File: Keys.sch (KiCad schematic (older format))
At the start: 144 parts, among them SW1 20, SW10 LEFT-SHIFT, SW11 41, SW12 51, SW13 22, SW14 32, SW15 42, SW16 52, SW17 02, SW18 12, SW19 03, SW2 30, SW20 13, SW21 23, SW22 33, SW23 43, SW24 53, SW25 24, SW26 34, SW28 54, SW29 04, SW3 40, SW30 14, SW31 05, SW32 15, SW33 25, SW34 35, SW35 45, SW37 26, SW38 36, SW39 46, SW4 50, SW40 56, SW41 06, SW42 16, SW43 07, SW44 17, SW45 27, SW46 37, SW48 57, SW49 28, SW5 00, SW50 38, SW51 48, SW52 58, SW53 08, SW54 18, SW55 09, SW56 19, SW57 29, SW58 39, SW59 49, SW6 10, SW60 59, SW61 010, SW62 110, SW63 210, SW64 310, SW65 410, SW66 510, SW67 011, SW68 111, SW69 211, SW7 01, SW70 311, SW71 411, SW72 511, SW8 11, SW9 21

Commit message: iterating
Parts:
- Backspace1: renamed from SW60; footprint CherryKeys:CHERRY_PCB_100H -> daprice-keyswitches:Stabilizer_MX_2u; symbol Keys-rescue:SWITCH_PUSH-Cherry-Symbol-chgray-keyboard-rescue -> Keys-rescue:SWITCH_PUSH-Cherry-Symbol-chgray-keyboard-rescue-Keys-rescue
- D1, D10, D11, D12, D13, D14, D15, D16, D17, D18, D19, D2, D20, D21, D22, D23, D24, D25, D26, D27, D28, D29, D3, D30, D31, D32, D33, D34, D35, D36, D37, D38, D39, D4, D40, D41, D42, D43, D44, D45, D46, D47, D48, D49, D5, D50, D51, D52, D53, D54, D55, D56, D57, D58, D59, D6, D60, D61, D62, D63, D64, D65, D66, D67, D68, D69, D7, D70, D71, D72, D8, D9: footprint CherryKeys:CHERRY_MX_DIODE -> Diode_SMD:D_SOD-123; symbol Keys-rescue:DIODE-Cherry-Symbol-chgray-keyboard-rescue -> Keys-rescue:DIODE-Cherry-Symbol-chgray-keyboard-rescue-Keys-rescue
- ENTER1: renamed from SW67; footprint CherryKeys:CHERRY_PCB_100H -> daprice-keyswitches:Stabilizer_MX_2u; symbol Keys-rescue:SWITCH_PUSH-Cherry-Symbol-chgray-keyboard-rescue -> Keys-rescue:SWITCH_PUSH-Cherry-Symbol-chgray-keyboard-rescue-Keys-rescue
- LEFT-SHIFT1: renamed from SW10; value LEFT-SHIFT -> 31; footprint CherryKeys:CHERRY_PCB_100H -> daprice-keyswitches:Stabilizer_MX_2u; symbol Keys-rescue:SWITCH_PUSH-Cherry-Symbol-chgray-keyboard-rescue -> Keys-rescue:SWITCH_PUSH-Cherry-Symbol-chgray-keyboard-rescue-Keys-rescue
- LEFT-SPACE1, RIGHT-SHIFT1, RIGHT-SHIFT2: footprint CherryKeys:CHERRY_PCB_100H -> daprice-keyswitches:Stabilizer_MX_2u; symbol Keys-rescue:SWITCH_PUSH-Cherry-Symbol-chgray-keyboard-rescue -> Keys-rescue:SWITCH_PUSH-Cherry-Symbol-chgray-keyboard-rescue-Keys-rescue
- SW1, SW11, SW12, SW13, SW14, SW15, SW16, SW17, SW18, SW19, SW2, SW20, SW21, SW22, SW23, SW24, SW25, SW26, SW28, SW29, SW3, SW30, SW31, SW32, SW33, SW34, SW35, SW37, SW38, SW39, SW4, SW40, SW41, SW42, SW43, SW44, SW45, SW46, SW48, SW49, SW5, SW50, SW51, SW52, SW53, SW54, SW55, SW56, SW57, SW58, SW59, SW6, SW61, SW62, SW63, SW64, SW65, SW66, SW68, SW69, SW7, SW70, SW71, SW72, SW8, SW9: footprint CherryKeys:CHERRY_PCB_100H -> daprice-keyswitches:Kailh_socket_MX; symbol Keys-rescue:SWITCH_PUSH-Cherry-Symbol-chgray-keyboard-rescue -> Keys-rescue:SWITCH_PUSH-Cherry-Symbol-chgray-keyboard-rescue-Keys-rescue
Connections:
- wire segments 368 -> 372

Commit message: add 1.75U switch
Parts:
- Backspace1, ENTER1, LEFT-SHIFT1, LEFT-SPACE1, RIGHT-SHIFT1, RIGHT-SHIFT2, SW11, SW12, SW13, SW14, SW15, SW16, SW17, SW18, SW19, SW2, SW20, SW21, SW22, SW23, SW24, SW25, SW26, SW28, SW29, SW3, SW30, SW31, SW32, SW33, SW34, SW35, SW37, SW38, SW39, SW4, SW40, SW41, SW42, SW43, SW44, SW45, SW46, SW48, SW49, SW5, SW50, SW51, SW52, SW53, SW54, SW55, SW56, SW57, SW58, SW59, SW6, SW61, SW62, SW63, SW64, SW65, SW66, SW68, SW69, SW7, SW70, SW71, SW72, SW8, SW9: symbol Keys-rescue:SWITCH_PUSH-Cherry-Symbol-chgray-keyboard-rescue-Keys-rescue -> Keys-rescue:SWITCH_PUSH-Cherry-Symbol-chgray-keyboard-rescue-Keys-rescue-Keys-rescue
- D1, D10, D11, D12, D13, D14, D15, D16, D17, D18, D19, D2, D20, D21, D22, D23, D24, D25, D26, D27, D28, D29, D3, D30, D31, D32, D33, D34, D35, D36, D37, D38, D39, D4, D40, D41, D42, D43, D44, D45, D46, D47, D48, D49, D5, D50, D51, D52, D53, D54, D55, D56, D57, D58, D59, D6, D60, D61, D62, D63, D64, D65, D66, D67, D68, D69, D7, D70, D71, D72, D8, D9: symbol Keys-rescue:DIODE-Cherry-Symbol-chgray-keyboard-rescue-Keys-rescue -> Keys-rescue:DIODE-Cherry-Symbol-chgray-keyboard-rescue-Keys-rescue-Keys-rescue
- SW1: footprint daprice-keyswitches:Kailh_socket_MX -> daprice-keyswitches:Stabilizer_MX_1.75u; symbol Keys-rescue:SWITCH_PUSH-Cherry-Symbol-chgray-keyboard-rescue-Keys-rescue -> Keys-rescue:SWITCH_PUSH-Cherry-Symbol-chgray-keyboard-rescue-Keys-rescue-Keys-rescue

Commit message: working
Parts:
- SW6: footprint daprice-keyswitches:Kailh_socket_MX -> daprice-keyswitches:Stabilizer_MX_1.5u
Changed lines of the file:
@@
 F 0 "SW6" H 2150 2110 50  0000 C CNN
 F 1 "10" H 2000 1920 50  0000 C CNN
-F 2 "daprice-keyswitches:Kailh_socket_MX" H 2000 2000 60  0001 C CNN
+F 2 "daprice-keyswitches:Stabilizer_MX_1.5u" H 2000 2000 60  0001 C CNN
 F 3 "" H 2000 2000 60  0001 C CNN
 	1    2000 2000

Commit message: working on rgb
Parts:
- added D73, D74, D75, D76, D77, D78, D79, D80, D81, D82, D83, D84: DIODE, Diode_SMD:D_SOD-123, symbol chgray-keyboard-rescue:DIODE-Cherry-Symbol-chgray-keyboard-rescue-Keys-rescue-K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
- added ENTER2, ENTER3: 011, daprice-keyswitches:Stabilizer_MX_1.75u, symbol chgray-keyboard-rescue:SWITCH_PUSH-Cherry-Symbol-chgray-keyboard-rescue-Keys-re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
- added SW1, SW36: 111, daprice-keyswitches:Kailh_socket_MX, symbol chgray-keyboard-rescue:SWITCH_PUSH-Cherry-Symbol-chgray-keyboard-rescue-Keys-re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
- added SW10, SW60: 311, daprice-keyswitches:Kailh_socket_MX, symbol chgray-keyboard-rescue:SWITCH_PUSH-Cherry-Symbol-chgray-keyboard-rescue-Keys-re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
- added SW15, SW67: 411, daprice-keyswitches:Kailh_socket_MX, symbol chgray-keyboard-rescue:SWITCH_PUSH-Cherry-Symbol-chgray-keyboard-rescue-Keys-re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
- added SW27, SW73: 511, daprice-keyswitches:Kailh_socket_MX, symbol chgray-keyboard-rescue:SWITCH_PUSH-Cherry-Symbol-chgray-keyboard-rescue-Keys-re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
- added SW47, SW6: 211, daprice-keyswitches:Kailh_socket_MX, symbol chgray-keyboard-rescue:SWITCH_PUSH-Cherry-Symbol-chgray-keyboard-rescue-Keys-re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
- Backspace1: footprint daprice-keyswitches:Stabilizer_MX_2u -> daprice-keyswitches:Stabilizer_MX_1.25u; symbol Keys-rescue:SWITCH_PUSH-Cherry-Symbol-chgray-keyboard-rescue-Keys-rescue-Keys-rescue -> chgray-keyboard-rescue:SWITCH_PUSH-Cherry-Symbol-chgray-keyboard-rescue-Keys-rescue-Keys-rescue-Keys-rescue
- CAPS1: renamed from SW1; footprint daprice-keyswitches:Stabilizer_MX_1.75u -> daprice-keyswitches:Stabilizer_MX_1.5u; symbol Keys-rescue:SWITCH_PUSH-Cherry-Symbol-chgray-keyboard-rescue-Keys-rescue-Keys-rescue -> chgray-keyboard-rescue:SWITCH_PUSH-Cherry-Symbol-chgray-keyboard-rescue-Keys-rescue-Keys-rescue-Keys-rescue
- D1, D10, D11, D12, D13, D14, D15, D16, D17, D18, D19, D2, D20, D21, D22, D23, D24, D25, D26, D27, D28, D29, D3, D30, D31, D32, D33, D34, D35, D36, D37, D38, D39, D4, D40, D41, D42, D43, D44, D45, D46, D47, D48, D49, D5, D50, D51, D52, D53, D54, D55, D56, D57, D58, D59, D6, D60, D61, D62, D63, D64, D65, D66, D67, D68, D69, D7, D70, D71, D72, D8, D9: symbol Keys-rescue:DIODE-Cherry-Symbol-chgray-keyboard-rescue-Keys-rescue-Keys-rescue -> chgray-keyboard-rescue:DIODE-Cherry-Symbol-chgray-keyboard-rescue-Keys-rescue-Keys-rescue-Keys-rescue
- ENTER1: footprint daprice-keyswitches:Stabilizer_MX_2u -> daprice-keyswitches:Stabilizer_MX_1.75u; symbol Keys-rescue:SWITCH_PUSH-Cherry-Symbol-chgray-keyboard-rescue-Keys-rescue-Keys-rescue -> chgray-keyboard-rescue:SWITCH_PUSH-Cherry-Symbol-chgray-keyboard-rescue-Keys-rescue-Keys-rescue-Keys-rescue
- LEFT-SHIFT1, SW11, SW12, SW13, SW14, SW16, SW17, SW18, SW19, SW2, SW20, SW21, SW22, SW23, SW24, SW25, SW26, SW28, SW29, SW3, SW30, SW31, SW32, SW33, SW34, SW35, SW37, SW38, SW39, SW4, SW40, SW41, SW42, SW43, SW44, SW45, SW46, SW48, SW49, SW5, SW50, SW51, SW52, SW53, SW54, SW55, SW56, SW57, SW58, SW59, SW61, SW62, SW63, SW64, SW65, SW66, SW68, SW69, SW7, SW70, SW71, SW72, SW8, SW9: symbol Keys-rescue:SWITCH_PUSH-Cherry-Symbol-chgray-keyboard-rescue-Keys-rescue-Keys-rescue -> chgray-keyboard-rescue:SWITCH_PUSH-Cherry-Symbol-chgray-keyboard-rescue-Keys-rescue-Keys-rescue-Keys-rescue
- LEFT-SPACE1, RIGHT-SHIFT1: footprint daprice-keyswitches:Stabilizer_MX_2u -> daprice-keyswitches:Stabilizer_MX_2.25u; symbol Keys-rescue:SWITCH_PUSH-Cherry-Symbol-chgray-keyboard-rescue-Keys-rescue-Keys-rescue -> chgray-keyboard-rescue:SWITCH_PUSH-Cherry-Symbol-chgray-keyboard-rescue-Keys-rescue-Keys-rescue-Keys-rescue
- RIGHT-SPACE1: renamed from RIGHT-SHIFT2; footprint daprice-keyswitches:Stabilizer_MX_2u -> daprice-keyswitches:Stabilizer_MX_2.25u; symbol Keys-rescue:SWITCH_PUSH-Cherry-Symbol-chgray-keyboard-rescue-Keys-rescue-Keys-rescue -> chgray-keyboard-rescue:SWITCH_PUSH-Cherry-Symbol-chgray-keyboard-rescue-Keys-rescue-Keys-rescue-Keys-rescue
- TAB1: renamed from SW6; footprint daprice-keyswitches:Stabilizer_MX_1.5u -> daprice-keyswitches:Stabilizer_MX_1.25u; symbol Keys-rescue:SWITCH_PUSH-Cherry-Symbol-chgray-keyboard-rescue-Keys-rescue-Keys-rescue -> chgray-keyboard-rescue:SWITCH_PUSH-Cherry-Symbol-chgray-keyboard-rescue-Keys-rescue-Keys-rescue-Keys-rescue
- WinKey1: renamed from SW15; footprint daprice-keyswitches:Kailh_socket_MX -> daprice-keyswitches:Stabilizer_MX_1.5u; symbol Keys-rescue:SWITCH_PUSH-Cherry-Symbol-chgray-keyboard-rescue-Keys-rescue-Keys-rescue -> chgray-keyboard-rescue:SWITCH_PUSH-Cherry-Symbol-chgray-keyboard-rescue-Keys-rescue-Keys-rescue-Keys-rescue
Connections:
- net labels added: KEY_COL12, KEY_COL13
- wire segments 372 -> 434

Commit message: rgb
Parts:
- S1: renamed from ENTER1; footprint daprice-keyswitches:Stabilizer_MX_1.75u -> daprice-keyswitches:Kailh_socket_MX
- S2: renamed from ENTER2; footprint daprice-keyswitches:Stabilizer_MX_1.75u -> daprice-keyswitches:Kailh_socket_MX
- S3: renamed from ENTER3; footprint daprice-keyswitches:Stabilizer_MX_1.75u -> daprice-keyswitches:Kailh_socket_MX
- renumbered SW2 to SW1, SW13 to SW10, SW14 to SW11, SW16 to SW12, SW17 to SW13, SW18 to SW14, SW19 to SW15, SW20 to SW16, SW21 to SW17, SW22 to SW18, SW23 to SW19, SW3 to SW2, SW24 to SW20, SW25 to SW21, SW26 to SW22, SW28 to SW23, SW29 to SW24, SW30 to SW25, SW31 to SW26, SW32 to SW27, SW33 to SW28, SW34 to SW29, SW4 to SW3, SW35 to SW30, SW37 to SW31, SW38 to SW32, SW39 to SW33, SW40 to SW34, SW41 to SW35, SW42 to SW36, SW43 to SW37, SW44 to SW38, SW45 to SW39, SW5 to SW4, SW46 to SW40, SW48 to SW41, SW49 to SW42, SW50 to SW43, SW51 to SW44, SW52 to SW45, SW53 to SW46, SW54 to SW47, SW55 to SW48, SW56 to SW49, SW7 to SW5, SW57 to SW50, SW58 to SW51, SW59 to SW52, SW61 to SW53, SW62 to SW54, SW63 to SW55, SW64 to SW56, SW65 to SW57, SW66 to SW58, SW68 to SW59, SW8 to SW6, SW69 to SW60, SW70 to SW61, SW71 to SW62, SW72 to SW63, SW1 to SW64, SW6 to SW65, SW10 to SW66, SW15 to SW67, SW27 to SW68, SW36 to SW69, SW9 to SW7, SW47 to SW70, SW60 to SW71, SW67 to SW72, SW11 to SW8, SW12 to SW9

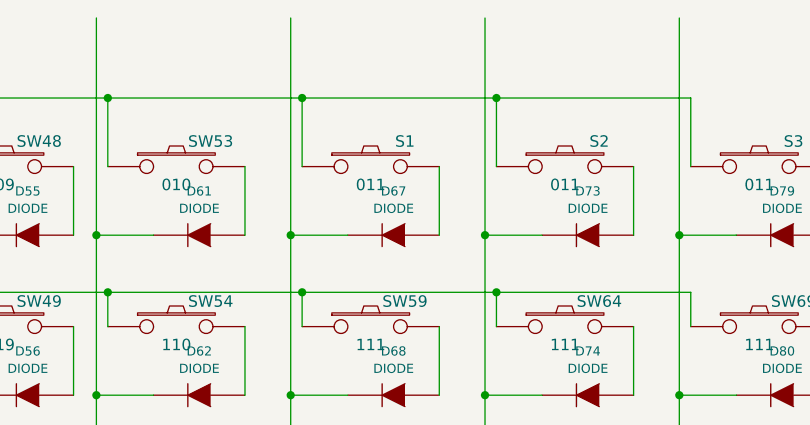
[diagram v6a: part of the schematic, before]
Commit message: laying out keyboard; all keys aligned!
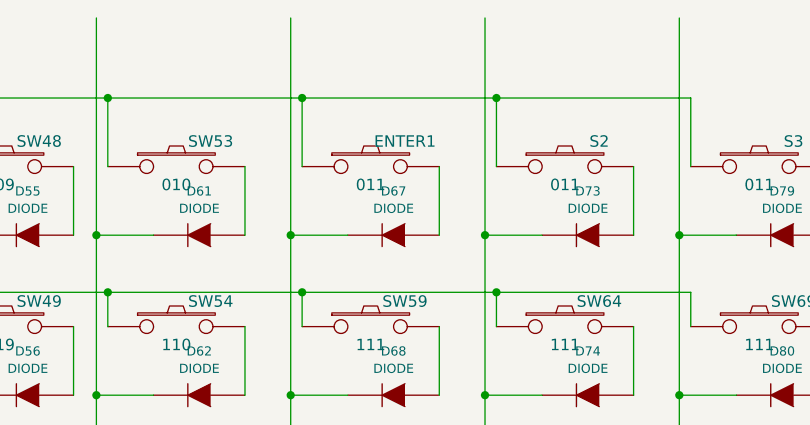
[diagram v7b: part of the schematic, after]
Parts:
- ENTER1: renamed from S1; footprint daprice-keyswitches:Kailh_socket_MX -> daprice-keyswitches:Stabilizer_MX_1.75u
- SW44: footprint daprice-keyswitches:Kailh_socket_MX -> daprice-keyswitches:Stabilizer_MX_1.25u
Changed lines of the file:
@@
 F 0 "SW44" H 9300 4960 50  0000 C CNN
 F 1 "48" H 9150 4770 50  0000 C CNN
-F 2 "daprice-keyswitches:Kailh_socket_MX" H 9150 4850 60  0001 C CNN
+F 2 "daprice-keyswitches:Stabilizer_MX_1.25u" H 9150 4850 60  0001 C CNN
 F 3 "" H 9150 4850 60  0001 C CNN
 	1    9150 4850
@@
 Connection ~ 10350 2300
 $Comp
-L chgray-keyboard-rescue:SWITCH_PUSH-Cherry-Symbol-chgray-keyboard-rescue-Keys-rescue-Keys-rescue-Keys-rescue S1
+L chgray-keyboard-rescue:SWITCH_PUSH-Cherry-Symbol-chgray-keyboard-rescue-Keys-rescue-Keys-rescue-Keys-rescue ENTER1
 U 1 1 60AE6AA1
 P 11550 1300
-F 0 "S1" H 11700 1410 50  0000 C CNN
+F 0 "ENTER1" H 11700 1410 50  0000 C CNN
 F 1 "011" H 11550 1220 50  0000 C CNN
-F 2 "daprice-keyswitches:Kailh_socket_MX" H 11550 1300 60  0001 C CNN
+F 2 "daprice-keyswitches:Stabilizer_MX_1.75u" H 11550 1300 60  0001 C CNN
 F 3 "" H 11550 1300 60  0001 C CNN
 	1    11550 1300

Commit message: Squashed commit of the following:
commit 82315f0ae1d56e508510c236d094091e5279ecfb
Author: Chris Gray (COSINE FUNDAMENTALS) <chgray@microsoft.com>
Date:   Sun May 9 12:30:08 2021 -0700

    remove pdf

commit 9829b40eb261ee4368c12e62176b20d48804d4ea
Author: Chris Gray (COSINE FUNDAMENTALS) <chgray@microsoft.com>
Date:   Sun May 9 12:06:55 2021 -0700

    add led fork

commit 28d4239d5e1579f8d8aedf2c60bdde25e23cad7c
Author: Chris Gray (COSINE FUNDAMENTALS) <chgray@microsoft.com>
Date:   Sun May 9 11:15:25 2021 -0700

    add led fork

commit 1ebadf8c3c77fdb13276f8c9b4483595e04fa1fa
Author: Chris Gray (COSINE FUNDAMENTALS) <chgray@microsoft.com>
Date:   Sun May 9 09:17:28 2021 -0700

    laying out keyboard; all keys aligned!

commit 209244f41c6b29d5d1d0d9d7c7194bf8aa42c4ce
Author: Chris Gray (COSINE FUNDAMENTALS) <chgray@microsoft.com>
Date:   Sun May 9 08:28:06 2021 -0700

    laying out keyboard; all keys aligned!

commit 9051df00b855818fb551d5add748e3f5ed9bac38
Author: Chris Gray (COSINE FUNDAMENTALS) <chgray@microsoft.com>
Date:   Sun May 9 07:49:34 2021 -0700

    laying out keyboard; all keys aligned!
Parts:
- SW4: symbol chgray-keyboard-rescue:SWITCH_PUSH-Cherry-Symbol-chgray-keyboard-rescue-Keys-rescue-Keys-rescue-Keys-rescue -> Cherry-Symbol:SWITCH_PUSH
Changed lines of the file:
@@
 KEY_COL10
 $Comp
-L chgray-keyboard-rescue:SWITCH_PUSH-Cherry-Symbol-chgray-keyboard-rescue-Keys-rescue-Keys-rescue-Keys-rescue SW4
+L Cherry-Symbol:SWITCH_PUSH SW4
 U 1 1 58964642
 P 2000 1300
